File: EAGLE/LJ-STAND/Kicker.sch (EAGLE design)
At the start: 7 parts, among them Q2 BUZ20

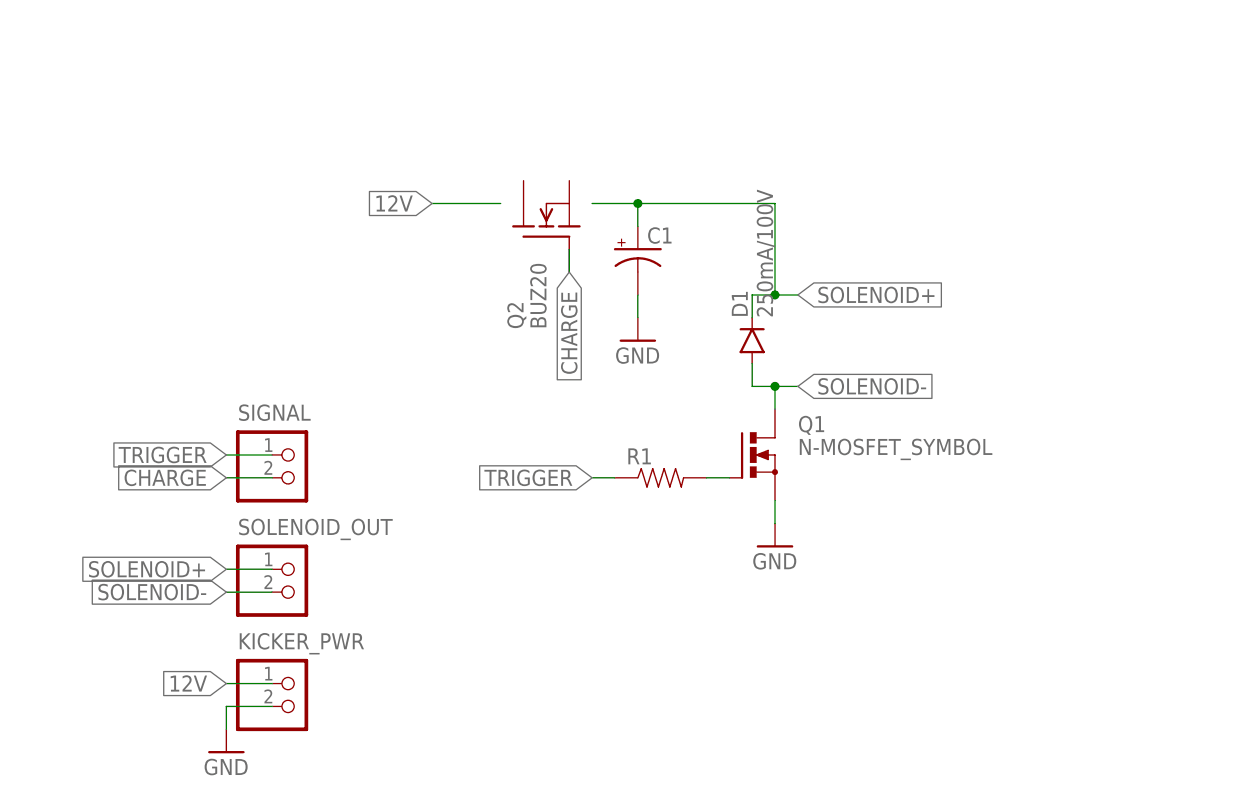
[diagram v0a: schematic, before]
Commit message: Solenoid circuit - added fet & relay and capacitor
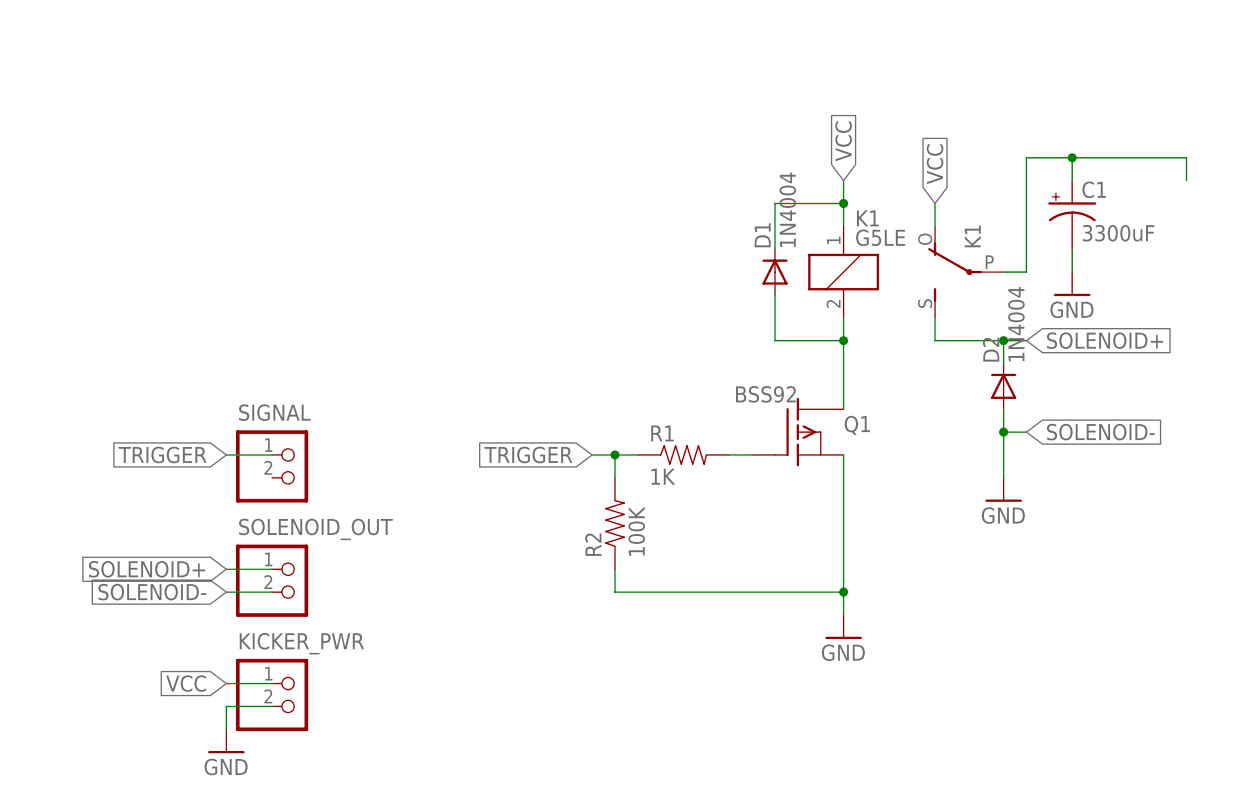
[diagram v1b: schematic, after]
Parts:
- removed Q2: BUZ20, transistor-fet:BUZ20
- added D2: 1N4004, diode:1N4004
- added K1: G5LE, relay:G5LE
- added Q1: BSS92, transistor-fet:BSS92
- added R2: 100K, SparkFun-Resistors:RESISTOR0805-RES
- C1: value (none) -> 3300uF; device SparkFun-Capacitors:CAP_POLPTH3 -> rcl:CPOL-USE10-22.5
- D1: value 250mA/100V -> 1N4004; device SparkFun-DiscreteSemi:DIODEBAS16 -> diode:1N4004
- R1: value (none) -> 1K; device SparkFun-Resistors:RESISTOR0805-RES -> SparkFun-Resistors:RESISTOR0603
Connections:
- removed net 12V: KICKER_PWR.1
- removed net CHARGE: SIGNAL.2
- new net N$3: D1.A, K11.2, Q1.D
- new net N$5: C1.+, K12.P
- new net VCC: D1.C, K11.1, K12.O, KICKER_PWR.1
- net GND: now also Q1.S, R2.1
- net N$2: now also Q1.G
- net SOLENOID+: now also D2.C, K12.S; no longer C1.+, D1.C
- net SOLENOID-: now also D2.A; no longer D1.A
- net TRIGGER: now also R2.2
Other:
- moved on the sheet: C1, R1
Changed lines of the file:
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@@
 <part name="GND1" library="supply1" deviceset="GND" device=""/>
 <part name="SIGNAL" library="jst-ph" deviceset="B2B-PH-*" device="K-S"/>
-<part name="R1" library="SparkFun-Resistors" deviceset="RESISTOR" device="0805-RES"/>
+<part name="R1" library="SparkFun-Resistors" deviceset="RESISTOR" device="0603" value="1K"/>
 <part name="GND2" library="supply1" deviceset="GND" device=""/>
-<part name="Q1" library="transistor-power" deviceset="N-MOSFET_SYMBOL" device=""/>
-<part name="D1" library="SparkFun-DiscreteSemi" deviceset="DIODE" device="BAS16" value="250mA/100V"/>
-<part name="C1" library="SparkFun-Capacitors" deviceset="CAP_POL" device="PTH3"/>
+<part name="Q1" library="transistor-fet" deviceset="BSS92" device=""/>
+<part name="R2" library="SparkFun-Resistors" deviceset="RESISTOR" device="0805-RES" value="100K"/>
+<part name="K1" library="relay" deviceset="G5LE" device=""/>
 <part name="GND3" library="supply1" deviceset="GND" device=""/>
-<part name="Q2" library="transistor-fet" deviceset="BUZ20" device=""/>
+<part name="C1" library="rcl" deviceset="CPOL-US" device="E10-22.5" value="3300uF"/>
+<part name="GND4" library="supply1" deviceset="GND" device=""/>
+<part name="D1" library="diode" deviceset="1N4004" device=""/>
+<part name="D2" library="diode" deviceset="1N4004" device=""/>
 </parts>
 <sheets>
@@
 <instance part="GND1" gate="1" x="7.62" y="73.66"/>
 <instance part="SIGNAL" gate="G$1" x="12.7" y="106.68"/>
-<instance part="R1" gate="G$1" x="55.88" y="104.14"/>
-<instance part="GND2" gate="1" x="68.58" y="96.52"/>
-<instance part="Q1" gate="G$1" x="66.04" y="106.68"/>
-<instance part="D1" gate="G$1" x="66.04" y="119.38" rot="R90"/>
-<instance part="C1" gate="G$1" x="53.34" y="129.54"/>
-<instance part="GND3" gate="1" x="53.34" y="119.38"/>
-<instance part="Q2" gate="G$1" x="43.18" y="132.08" rot="R90"/>
+<instance part="R1" gate="G$1" x="58.42" y="106.68"/>
+<instance part="GND2" gate="1" x="76.2" y="86.36"/>
+<instance part="Q1" gate="G$1" x="71.12" y="109.22" smashed="yes">
+<attribute name="NAME" x="76.2" y="109.22" size="1.778" layer="95"/>
+<attribute name="VALUE" x="71.12" y="114.3" size="1.778" layer="96" rot="R180"/>
+</instance>
+<instance part="R2" gate="G$1" x="50.8" y="99.06" rot="R90"/>
+<instance part="K1" gate="1" x="76.2" y="127"/>
+<instance part="K1" gate="2" x="91.44" y="127" rot="R90"/>
+<instance part="GND3" gate="1" x="93.98" y="101.6"/>
+<instance part="C1" gate="G$1" x="101.6" y="134.62"/>
+<instance part="GND4" gate="1" x="101.6" y="124.46"/>
+<instance part="D1" gate="1" x="68.58" y="127" rot="R90"/>
+<instance part="D2" gate="1" x="93.98" y="114.3" rot="R90"/>
 </instances>
 <busses>
@@
 </segment>
 <segment>
-<pinref part="D1" gate="G$1" pin="C"/>
-<wire x1="66.04" y1="121.92" x2="66.04" y2="124.46" width="0.1524" layer="91"/>
-<wire x1="66.04" y1="124.46" x2="68.58" y2="124.46" width="0.1524" layer="91"/>
-<label x="71.12" y="124.46" size="1.778" layer="95" xref="yes"/>
-<wire x1="68.58" y1="124.46" x2="71.12" y2="124.46" width="0.1524" layer="91"/>
-<wire x1="68.58" y1="134.62" x2="68.58" y2="124.46" width="0.1524" layer="91"/>
-<pinref part="C1" gate="G$1" pin="+"/>
-<wire x1="53.34" y1="132.08" x2="53.34" y2="134.62" width="0.1524" layer="91"/>
-<wire x1="53.34" y1="134.62" x2="68.58" y2="134.62" width="0.1524" layer="91"/>
-<junction x="68.58" y="124.46"/>
-<wire x1="53.34" y1="134.62" x2="48.26" y2="134.62" width="0.1524" layer="91"/>
-<junction x="53.34" y="134.62"/>
+<pinref part="K1" gate="2" pin="S"/>
+<wire x1="86.36" y1="121.92" x2="86.36" y2="119.38" width="0.1524" layer="91"/>
+<wire x1="86.36" y1="119.38" x2="93.98" y2="119.38" width="0.1524" layer="91"/>
+<label x="96.52" y="119.38" size="1.778" layer="95" xref="yes"/>
+<pinref part="D2" gate="1" pin="C"/>
+<wire x1="93.98" y1="119.38" x2="96.52" y2="119.38" width="0.1524" layer="91"/>
+<wire x1="93.98" y1="116.84" x2="93.98" y2="119.38" width="0.1524" layer="91"/>
+<junction x="93.98" y="119.38"/>
 </segment>
 </net>
@@
 </segment>
 <segment>
-<wire x1="68.58" y1="111.76" x2="68.58" y2="114.3" width="0.1524" layer="91"/>
-<wire x1="71.12" y1="114.3" x2="68.58" y2="114.3" width="0.1524" layer="91"/>
-<wire x1="68.58" y1="114.3" x2="66.04" y2="114.3" width="0.1524" layer="91"/>
-<pinref part="D1" gate="G$1" pin="A"/>
-<wire x1="66.04" y1="114.3" x2="66.04" y2="116.84" width="0.1524" layer="91"/>
-<label x="71.12" y="114.3" size="1.778" layer="95" xref="yes"/>
-<junction x="68.58" y="114.3"/>
+<pinref part="GND3" gate="1" pin="GND"/>
+<wire x1="93.98" y1="109.22" x2="96.52" y2="109.22" width="0.1524" layer="91"/>
+<wire x1="93.98" y1="109.22" x2="93.98" y2="104.14" width="0.1524" layer="91"/>
+<label x="96.52" y="109.22" size="1.778" layer="95" xref="yes"/>
+<pinref part="D2" gate="1" pin="A"/>
+<wire x1="93.98" y1="109.22" x2="93.98" y2="111.76" width="0.1524" layer="91"/>
+<junction x="93.98" y="109.22"/>
 </segment>
 </net>
@@
 <segment>
 <pinref part="C1" gate="G$1" pin="-"/>
-<wire x1="53.34" y1="124.46" x2="53.34" y2="121.92" width="0.1524" layer="91"/>
-<pinref part="GND3" gate="1" pin="GND"/>
-</segment>
-</net>
-<net name="12V" class="0">
-<segment>
-<pinref part="KICKER_PWR" gate="G$1" pin="1"/>
-<wire x1="12.7" y1="81.28" x2="7.62" y2="81.28" width="0.1524" layer="91"/>
-<label x="7.62" y="81.28" size="1.778" layer="95" rot="R180" xref="yes"/>
+<wire x1="101.6" y1="129.54" x2="101.6" y2="127" width="0.1524" layer="91"/>
+<pinref part="GND4" gate="1" pin="GND"/>
 </segment>
 <segment>
-<wire x1="38.1" y1="134.62" x2="30.48" y2="134.62" width="0.1524" layer="91"/>
-<label x="30.48" y="134.62" size="1.778" layer="95" rot="R180" xref="yes"/>
+<pinref part="Q1" gate="G$1" pin="S"/>
+<pinref part="GND2" gate="1" pin="GND"/>
+<wire x1="76.2" y1="106.68" x2="76.2" y2="91.44" width="0.1524" layer="91"/>
+<pinref part="R2" gate="G$1" pin="1"/>
+<wire x1="76.2" y1="91.44" x2="76.2" y2="88.9" width="0.1524" layer="91"/>
+<wire x1="50.8" y1="93.98" x2="50.8" y2="91.44" width="0.1524" layer="91"/>
+<wire x1="50.8" y1="91.44" x2="76.2" y2="91.44" width="0.1524" layer="91"/>
+<junction x="76.2" y="91.44"/>
 </segment>
 </net>
@@
 </segment>
 <segment>
+<pinref part="R2" gate="G$1" pin="2"/>
+<wire x1="50.8" y1="104.14" x2="50.8" y2="106.68" width="0.1524" layer="91"/>
 <pinref part="R1" gate="G$1" pin="1"/>
-<wire x1="50.8" y1="104.14" x2="48.26" y2="104.14" width="0.1524" layer="91"/>
-<label x="48.26" y="104.14" size="1.778" layer="95" rot="R180" xref="yes"/>
+<wire x1="53.34" y1="106.68" x2="50.8" y2="106.68" width="0.1524" layer="91"/>
+<wire x1="48.26" y1="106.68" x2="50.8" y2="106.68" width="0.1524" layer="91"/>
+<junction x="50.8" y="106.68"/>
+<label x="48.26" y="106.68" size="1.778" layer="95" rot="R180" xref="yes"/>
 </segment>
 </net>
-<net name="CHARGE" class="0">
+<net name="N$3" class="0">
 <segment>
-<pinref part="SIGNAL" gate="G$1" pin="2"/>
-<wire x1="12.7" y1="104.14" x2="7.62" y2="104.14" width="0.1524" layer="91"/>
-<label x="7.62" y="104.14" size="1.778" layer="95" rot="R180" xref="yes"/>
+<wire x1="76.2" y1="119.38" x2="68.58" y2="119.38" width="0.1524" layer="91"/>
+<pinref part="D1" gate="1" pin="A"/>
+<wire x1="68.58" y1="119.38" x2="68.58" y2="124.46" width="0.1524" layer="91"/>
+<pinref part="K1" gate="1" pin="2"/>
+<pinref part="Q1" gate="G$1" pin="D"/>
+<wire x1="76.2" y1="121.92" x2="76.2" y2="119.38" width="0.1524" layer="91"/>
+<junction x="76.2" y="119.38"/>
+<wire x1="76.2" y1="119.38" x2="76.2" y2="111.76" width="0.1524" layer="91"/>
+</segment>
+</net>
+<net name="N$5" class="0">
+<segment>
+<pinref part="K1" gate="2" pin="P"/>
+<wire x1="93.98" y1="127" x2="96.52" y2="127" width="0.1524" layer="91"/>
+<wire x1="96.52" y1="127" x2="96.52" y2="139.7" width="0.1524" layer="91"/>
+<wire x1="96.52" y1="139.7" x2="101.6" y2="139.7" width="0.1524" layer="91"/>
+<pinref part="C1" gate="G$1" pin="+"/>
+<wire x1="101.6" y1="137.16" x2="101.6" y2="139.7" width="0.1524" layer="91"/>
+<wire x1="101.6" y1="139.7" x2="114.3" y2="139.7" width="0.1524" layer="91"/>
+<junction x="101.6" y="139.7"/>
+<wire x1="114.3" y1="139.7" x2="114.3" y2="137.16" width="0.1524" layer="91"/>
+</segment>
+</net>
+<net name="VCC" class="0">
+<segment>
+<pinref part="K1" gate="2" pin="O"/>
+<wire x1="86.36" y1="132.08" x2="86.36" y2="134.62" width="0.1524" layer="91"/>
+<label x="86.36" y="134.62" size="1.778" layer="95" rot="R90" xref="yes"/>
 </segment>
 <segment>
-<wire x1="45.72" y1="129.54" x2="45.72" y2="127" width="0.1524" layer="91"/>
-<label x="45.72" y="127" size="1.778" layer="95" rot="R270" xref="yes"/>
+<pinref part="KICKER_PWR" gate="G$1" pin="1"/>
+<wire x1="12.7" y1="81.28" x2="7.62" y2="81.28" width="0.1524" layer="91"/>
+<label x="7.62" y="81.28" size="1.778" layer="95" rot="R180" xref="yes"/>
+</segment>
+<segment>
+<pinref part="K1" gate="1" pin="1"/>
+<wire x1="76.2" y1="132.08" x2="76.2" y2="134.62" width="0.1524" layer="91"/>
+<wire x1="76.2" y1="134.62" x2="76.2" y2="137.16" width="0.1524" layer="91"/>
+<wire x1="76.2" y1="134.62" x2="68.58" y2="134.62" width="0.1524" layer="91"/>
+<junction x="76.2" y="134.62"/>
+<pinref part="D1" gate="1" pin="C"/>
+<wire x1="68.58" y1="129.54" x2="68.58" y2="134.62" width="0.1524" layer="91"/>
+<label x="76.2" y="137.16" size="1.778" layer="95" rot="R90" xref="yes"/>
 </segment>
 </net>
@@
 <segment>
 <pinref part="R1" gate="G$1" pin="2"/>
-<wire x1="60.96" y1="104.14" x2="63.5" y2="104.14" width="0.1524" layer="91"/>
+<pinref part="Q1" gate="G$1" pin="G"/>
+<wire x1="63.5" y1="106.68" x2="66.04" y2="106.68" width="0.1524" layer="91"/>
 </segment>
 </net>
-<net name="N$1" class="0">
-<segment>
-<wire x1="68.58" y1="101.6" x2="68.58" y2="99.06" width="0.1524" layer="91"/>
-<pinref part="GND2" gate="1" pin="GND"/>
-</segment>
-</net>

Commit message: Hexagon too small
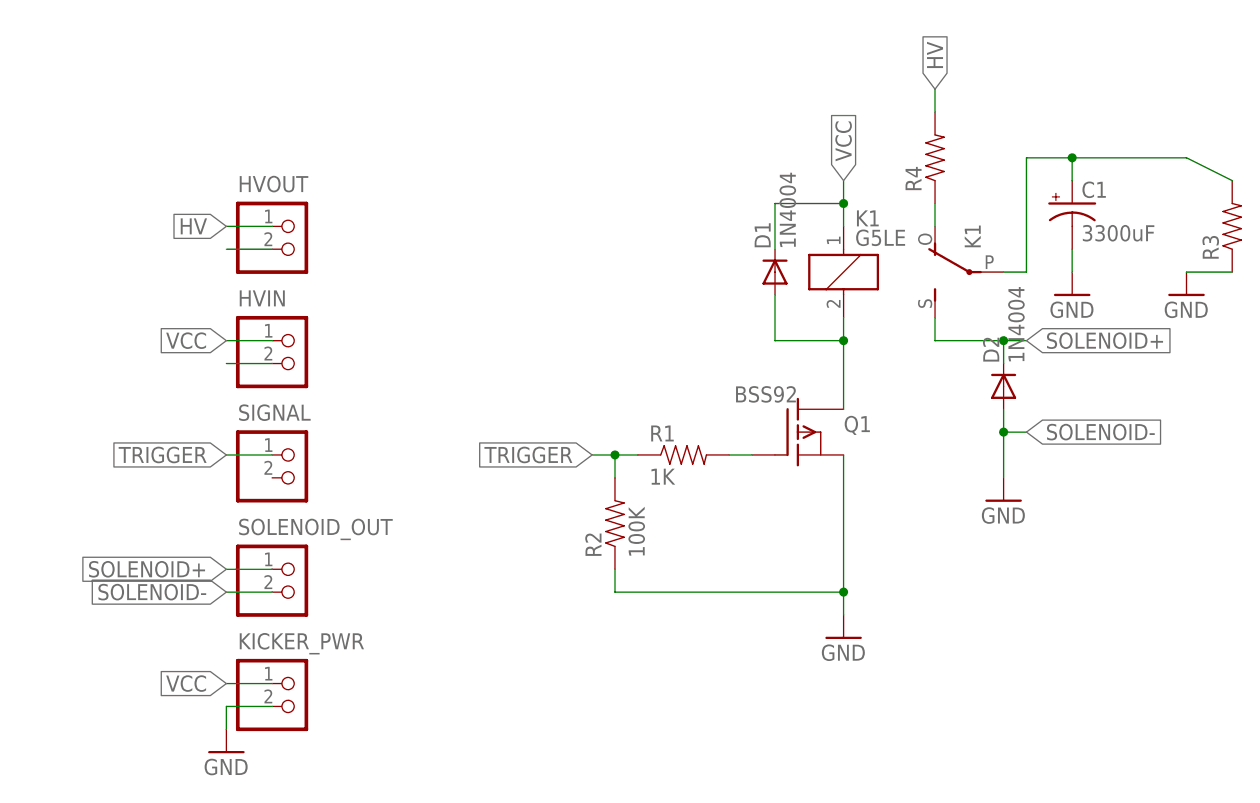
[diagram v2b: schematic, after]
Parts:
- added HVIN, HVOUT: (no value), jst-vh:B2P-VH
- added R3, R4: (no value), SparkFun-Resistors:RESISTORPTH-2W
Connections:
- new net HV: HVOUT.1, R4.2
- new net N$1: K12.O, R4.1
- new net N$4: HVOUT.2
- new net N$7: HVIN.2
- net GND: now also R3.1
- net N$5: now also R3.2
- net VCC: now also HVIN.1; no longer K12.O
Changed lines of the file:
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@@
 <part name="D1" library="diode" deviceset="1N4004" device=""/>
 <part name="D2" library="diode" deviceset="1N4004" device=""/>
+<part name="R3" library="SparkFun-Resistors" deviceset="RESISTOR" device="PTH-2W"/>
+<part name="GND5" library="supply1" deviceset="GND" device=""/>
+<part name="HVIN" library="jst-vh" deviceset="B2P-VH" device=""/>
+<part name="HVOUT" library="jst-vh" deviceset="B2P-VH" device=""/>
+<part name="R4" library="SparkFun-Resistors" deviceset="RESISTOR" device="PTH-2W"/>
 </parts>
 <sheets>
@@
 <instance part="D1" gate="1" x="68.58" y="127" rot="R90"/>
 <instance part="D2" gate="1" x="93.98" y="114.3" rot="R90"/>
+<instance part="R3" gate="G$1" x="119.38" y="132.08" rot="R90"/>
+<instance part="GND5" gate="1" x="114.3" y="124.46"/>
+<instance part="HVIN" gate="G$1" x="12.7" y="119.38"/>
+<instance part="HVOUT" gate="G$1" x="12.7" y="132.08"/>
+<instance part="R4" gate="G$1" x="86.36" y="139.7" rot="R90"/>
 </instances>
 <busses>
@@
 <junction x="76.2" y="91.44"/>
 </segment>
+<segment>
+<pinref part="R3" gate="G$1" pin="1"/>
+<pinref part="GND5" gate="1" pin="GND"/>
+<wire x1="119.38" y1="127" x2="114.3" y2="127" width="0.1524" layer="91"/>
+</segment>
 </net>
 <net name="TRIGGER" class="0">
@@
 <wire x1="101.6" y1="139.7" x2="114.3" y2="139.7" width="0.1524" layer="91"/>
 <junction x="101.6" y="139.7"/>
-<wire x1="114.3" y1="139.7" x2="114.3" y2="137.16" width="0.1524" layer="91"/>
+<wire x1="114.3" y1="139.7" x2="119.38" y2="137.16" width="0.1524" layer="91"/>
+<pinref part="R3" gate="G$1" pin="2"/>
 </segment>
 </net>
 <net name="VCC" class="0">
-<segment>
-<pinref part="K1" gate="2" pin="O"/>
-<wire x1="86.36" y1="132.08" x2="86.36" y2="134.62" width="0.1524" layer="91"/>
-<label x="86.36" y="134.62" size="1.778" layer="95" rot="R90" xref="yes"/>
-</segment>
 <segment>
 <pinref part="KICKER_PWR" gate="G$1" pin="1"/>
@@
 <label x="76.2" y="137.16" size="1.778" layer="95" rot="R90" xref="yes"/>
 </segment>
+<segment>
+<pinref part="HVIN" gate="G$1" pin="1"/>
+<wire x1="12.7" y1="119.38" x2="7.62" y2="119.38" width="0.1524" layer="91"/>
+<label x="7.62" y="119.38" size="1.778" layer="95" rot="R180" xref="yes"/>
+</segment>
 </net>
 <net name="N$2" class="0">
@@
 </segment>
 </net>
+<net name="HV" class="0">
+<segment>
+<pinref part="HVOUT" gate="G$1" pin="1"/>
+<wire x1="12.7" y1="132.08" x2="7.62" y2="132.08" width="0.1524" layer="91"/>
+<label x="7.62" y="132.08" size="1.778" layer="95" rot="R180" xref="yes"/>
+</segment>
+<segment>
+<pinref part="R4" gate="G$1" pin="2"/>
+<wire x1="86.36" y1="144.78" x2="86.36" y2="147.32" width="0.1524" layer="91"/>
+<label x="86.36" y="147.32" size="1.778" layer="95" rot="R90" xref="yes"/>
+</segment>
+</net>
+<net name="N$4" class="0">
+<segment>
+<pinref part="HVOUT" gate="G$1" pin="2"/>
+<wire x1="12.7" y1="129.54" x2="7.62" y2="129.54" width="0.1524" layer="91"/>
+</segment>
+</net>
+<net name="N$7" class="0">
+<segment>
+<pinref part="HVIN" gate="G$1" pin="2"/>
+<wire x1="12.7" y1="116.84" x2="7.62" y2="116.84" width="0.1524" layer="91"/>
+</segment>
+</net>
+<net name="N$1" class="0">
+<segment>
+<pinref part="K1" gate="2" pin="O"/>
+<pinref part="R4" gate="G$1" pin="1"/>
+<wire x1="86.36" y1="132.08" x2="86.36" y2="134.62" width="0.1524" layer="91"/>
+</segment>
+</net>
